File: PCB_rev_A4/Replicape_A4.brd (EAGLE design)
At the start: 100 x 69.6 mm, 189 parts, among them P8 F-2X23-, P9 F-2X23-, Q1 AON6758, Q2 AON6758, Q3 AON6758, Q4 NIF5002, Q5 NIF5002, Q6 NIF5002, U1 SN74AHC595PW, U10 RT8268, U11 PCA9685PW, U12 DAC088S085, U13 DRV8825PWP, U14 DRV8825PWP, U15 DRV8825PWP, U16 DRV8825PWP, U17 DRV8825PWP, U18 CAT24C256, U2 SN74AHC595PW, U3 SN74AHC595PW, U4 SN74AHC595PW, U5 SN74AHC595PW, U6 MCP16321, U7 MCP1402, U8 MCP1402, U9 MCP1402, X1 22-05-7028-02, X10 22-05-7028-02, X11 22-05-7028-02, X12 22-05-7038-03, X13 22-05-7028-02, X14 22-05-7048-04, X15 22-05-7048-04, X16 22-05-7048-04, X17 22-05-7048-04, X18 22-05-7048-04, X19 22-05-7028-02, X2 MSTBA4, X20 MSTBA4, X21 MSTBA2, X23 22-05-7028-02, X3 MSTBA2, X4 22-05-7028-02, X5 22-05-7028-02, X6 22-05-7028-02, X7 22-05-7038-03, X8 22-05-7038-03, X9 22-05-7038-03

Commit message: moved C31
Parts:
- moved R45 1.98 mm to (14.8, 6.14)
- moved LED8 1.83 mm to (14.8, 4.67)
- moved C31 1.30 mm to (22.0, 19.5)
- moved C12 1.02 mm to (18.1, 13.6)
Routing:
- net VDD_IN: track 239.4 -> 242.4 mm
- net DIR_X: track 67.9 -> 68.9 mm
- net GND: vias 194 -> 196
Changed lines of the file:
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@@
 <layer number="42" name="bRestrict" color="1" fill="10" visible="yes" active="yes"/>
 <layer number="43" name="vRestrict" color="2" fill="10" visible="yes" active="yes"/>
-<layer number="44" name="Drills" color="7" fill="1" visible="no" active="yes"/>
+<layer number="44" name="Drills" color="7" fill="1" visible="yes" active="yes"/>
 <layer number="45" name="Holes" color="7" fill="1" visible="yes" active="yes"/>
 <layer number="46" name="Milling" color="3" fill="1" visible="yes" active="yes"/>
@@
 <attribute name="NAME" x="31.0944" y="20.359" size="0.6096" layer="25" rot="R270"/>
 </element>
-<element name="C31" library="rcl" package="C0402" value="0.1uF" x="21.844" y="18.2254" smashed="yes" rot="R270">
-<attribute name="NAME" x="22.4576" y="18.76" size="0.6096" layer="25"/>
+<element name="C31" library="rcl" package="C0402" value="0.1uF" x="21.971" y="19.5208" smashed="yes" rot="R270">
+<attribute name="NAME" x="22.5846" y="20.0554" size="0.6096" layer="25"/>
 </element>
 <element name="C32" library="rcl" package="C0603" value="4.7uF" x="42.625" y="19.4" smashed="yes" rot="R270">
@@
 <attribute name="OC_NEWARK" value="unknown" x="92.625" y="47.875" size="1.778" layer="27" display="off"/>
 </element>
-<element name="C12" library="rcl" package="140CLH-0810" value="100uF" x="18.4" y="14.55" smashed="yes" rot="R90">
-<attribute name="NAME" x="16.745" y="20.235" size="1.27" layer="25" rot="R90"/>
+<element name="C12" library="rcl" package="140CLH-0810" value="100uF" x="18.0698" y="13.5848" smashed="yes" rot="R90">
+<attribute name="NAME" x="16.4148" y="19.2698" size="1.27" layer="25" rot="R90"/>
 </element>
 <element name="C27" library="rcl" package="C0402" value="0.1uF" x="28.7094" y="19.5208" smashed="yes" rot="R270">
@@
 </element>
 <element name="LOGO1" library="ohw-logo" package="OSHW_FILLX200_NOTEXT" value="OSHW_LOGO_FILLX0200-NT" x="43.2584" y="45.9602"/>
-<element name="LED8" library="led" package="CHIP-LED0603" value="red" x="14.875" y="6.5" smashed="yes" rot="R270">
-<attribute name="NAME" x="13.94" y="5.01" size="0.6096" layer="25"/>
+<element name="LED8" library="led" package="CHIP-LED0603" value="red" x="14.7734" y="4.6712" smashed="yes" rot="R270">
+<attribute name="NAME" x="16.2006" y="4.4512" size="0.6096" layer="25"/>
 </element>
-<element name="R45" library="rcl" package="R0402" value="4.7K" x="14.875" y="8.125" smashed="yes">
-<attribute name="NAME" x="16.215" y="8.01" size="0.6096" layer="25"/>
+<element name="R45" library="rcl" package="R0402" value="4.7K" x="14.7734" y="6.1438" smashed="yes">
+<attribute name="NAME" x="16.2658" y="5.851" size="0.6096" layer="25"/>
 </element>
 <element name="F1" library="SparkFun" package="3557" value="3557" x="9.775" y="11.85" rot="R90"/>
@@
 <contactref element="C23" pad="2"/>
 <contactref element="C25" pad="2"/>
-<wire x1="75.725" y1="51.3" x2="75.625" y2="49.125" width="0" layer="19" extent="1-1"/>
+<via x="73.72" y="54.0272" extent="1-16" drill="0.6"/>
+<via x="73.7454" y="52.9096" extent="1-16" drill="0.6"/>
 </signal>
 <signal name="SYS_5V">
@@
 <via x="48.875" y="3.125" extent="1-16" drill="0.3048"/>
 <wire x1="22.125" y1="26.65" x2="22.125" y2="26.625" width="0.1524" layer="1"/>
-<wire x1="22.125" y1="22.375" x2="22.125" y2="26.65" width="0.1524" layer="16"/>
-<wire x1="20.25" y1="20.5" x2="22.125" y2="22.375" width="0.1524" layer="16"/>
-<wire x1="20.25" y1="5" x2="20.25" y2="20.5" width="0.1524" layer="16"/>
-<wire x1="22.125" y1="3.125" x2="20.25" y2="5" width="0.1524" layer="16"/>
+<wire x1="22.125" y1="22.3028" x2="22.125" y2="26.65" width="0.1524" layer="16"/>
+<wire x1="22.125" y1="3.125" x2="20.2438" y2="5.0062" width="0.1524" layer="16"/>
 <via x="22.125" y="26.65" extent="1-16" drill="0.3048"/>
 <contactref element="P8" pad="26"/>
 <wire x1="55.75" y1="9.375" x2="55.835" y2="9.355" width="0.1524" layer="1"/>
+<wire x1="22.125" y1="22.3028" x2="20.9296" y2="21.1074" width="0.1524" layer="16"/>
+<wire x1="20.9296" y1="21.1074" x2="20.1676" y2="21.1074" width="0.1524" layer="16"/>
+<wire x1="20.1676" y1="21.1074" x2="19.6342" y2="20.574" width="0.1524" layer="16"/>
+<wire x1="19.6342" y1="20.574" x2="19.6342" y2="19.4056" width="0.1524" layer="16"/>
+<wire x1="19.6342" y1="19.4056" x2="20.2438" y2="18.796" width="0.1524" layer="16"/>
+<wire x1="20.2438" y1="18.796" x2="20.2438" y2="5.0062" width="0.1524" layer="16"/>
 </signal>
 <signal name="STEP_X">
@@
 <wire x1="13.125" y1="18" x2="14.125" y2="18" width="2" layer="1"/>
 <wire x1="14.125" y1="18" x2="17.125" y2="18" width="2" layer="1"/>
-<wire x1="17.125" y1="18" x2="18.4" y2="17.8" width="0.4" layer="1"/>
 <polygon width="0.1542" layer="1" isolate="0.5">
 <vertex x="13.375" y="11.5"/>
@@
 <vertex x="13.375" y="21.75"/>
 </polygon>
-<wire x1="14.225" y1="8.125" x2="14.125" y2="8.125" width="0.4" layer="1"/>
+<wire x1="14.1234" y1="6.1438" x2="14.125" y2="8.125" width="0.4" layer="1"/>
 <wire x1="14.125" y1="18" x2="14.125" y2="8.125" width="0.4" layer="1"/>
-<wire x1="17.125" y1="17.75" x2="18.4" y2="17.8" width="0.4" layer="1"/>
+<wire x1="17.125" y1="17.75" x2="18.0698" y2="16.8348" width="0.4" layer="1"/>
 <wire x1="52.525" y1="20.1" x2="51.75" y2="20.125" width="1.4224" layer="16"/>
 <wire x1="51.75" y1="20.125" x2="51.625" y2="20.125" width="0.8192" layer="16"/>
@@
 <wire x1="39.625" y1="20.125" x2="34.5" y2="20.125" width="1.4224" layer="16"/>
 <wire x1="34.5" y1="20.125" x2="27.625" y2="20.125" width="1.4224" layer="16"/>
-<wire x1="27.625" y1="20.125" x2="21.875" y2="20.125" width="1.4224" layer="16"/>
-<via x="21.875" y="20.125" extent="1-16" drill="0.6"/>
+<wire x1="27.625" y1="20.125" x2="20.6812" y2="20.125" width="1.4224" layer="16"/>
+<via x="20.6812" y="20.125" extent="1-16" drill="0.6"/>
 <wire x1="39.375" y1="20.375" x2="39.375" y2="21.75" width="0.4096" layer="1"/>
 <wire x1="39.625" y1="20.125" x2="39.375" y2="20.375" width="0.4096" layer="1"/>
@@
 <wire x1="80.25" y1="46.75" x2="80.225" y2="46.7" width="0.1524" layer="1"/>
 <wire x1="80.25" y1="47.125" x2="80.225" y2="47.2" width="0.1524" layer="1"/>
-<wire x1="18.75" y1="18.125" x2="18.4" y2="17.8" width="0.1524" layer="1"/>
 <wire x1="83.25" y1="47.25" x2="83.75" y2="47.25" width="0.254" layer="1"/>
 <wire x1="83.75" y1="47.25" x2="83.875" y2="47.125" width="0.254" layer="1"/>
@@
 <via x="60.875" y="49.375" extent="1-16" drill="0.305"/>
 <via x="77.75" y="40.625" extent="1-16" drill="0.7"/>
-<wire x1="22.875" y1="21.125" x2="22.875" y2="21.75" width="0.4064" layer="1"/>
-<wire x1="21.875" y1="20.125" x2="22.875" y2="21.125" width="0.4064" layer="1"/>
+<wire x1="22.875" y1="20.521" x2="22.875" y2="21.75" width="0.4064" layer="1"/>
 <wire x1="22.875" y1="21.75" x2="22.85" y2="21.7875" width="0.4064" layer="1"/>
 <polygon width="0.1542" layer="16" isolate="0.5">
@@
 <wire x1="27.625" y1="20.125" x2="28.7094" y2="20.125" width="0.4096" layer="1"/>
 <wire x1="28.7094" y1="20.125" x2="28.7094" y2="20.1708" width="0.4096" layer="1"/>
-<wire x1="21.875" y1="20.125" x2="21.844" y2="20.125" width="0.4096" layer="1"/>
-<wire x1="21.844" y1="20.125" x2="21.844" y2="18.8754" width="0.4096" layer="1"/>
 <wire x1="22.85" y1="21.7875" x2="22.85" y2="22.55" width="0.1524" layer="1"/>
 <wire x1="22.85" y1="22.55" x2="20" y2="25.4" width="0.1524" layer="1"/>
@@
 <wire x1="56.2" y1="26.6" x2="55.375" y2="26.6" width="0.1524" layer="1"/>
 <wire x1="55.375" y1="26.6" x2="55.3504" y2="26.9278" width="0.1524" layer="1"/>
-<wire x1="18.75" y1="18.125" x2="18.75" y2="18.55" width="1.4224" layer="1"/>
-<wire x1="18.75" y1="18.55" x2="20.3" y2="20.1" width="1.4224" layer="1"/>
-<wire x1="20.3" y1="20.1" x2="21.85" y2="20.1" width="1.4224" layer="1"/>
-<wire x1="21.85" y1="20.1" x2="21.875" y2="20.125" width="1.4224" layer="1"/>
 <wire x1="79.375" y1="39" x2="81" y2="39" width="0.8128" layer="1"/>
 <wire x1="81" y1="39" x2="81" y2="29.4" width="0.8128" layer="1"/>
@@
 <wire x1="79.289" y1="23.717" x2="79.195" y2="23.717" width="0.8128" layer="1"/>
 <wire x1="79.195" y1="23.717" x2="79.1" y2="23.622" width="0.8128" layer="1"/>
+<wire x1="17.125" y1="18" x2="18.0698" y2="18" width="1.9812" layer="1"/>
+<wire x1="18.0698" y1="18" x2="18.0698" y2="16.8348" width="1.9812" layer="1"/>
+<wire x1="20.6248" y1="20.125" x2="20.1948" y2="20.125" width="1.4224" layer="1"/>
+<wire x1="20.1948" y1="20.125" x2="18.0698" y2="18" width="1.4224" layer="1"/>
+<wire x1="22.875" y1="20.521" x2="22.479" y2="20.125" width="0.4064" layer="1"/>
+<wire x1="22.479" y1="20.125" x2="22.0168" y2="20.125" width="0.4064" layer="1"/>
+<wire x1="22.0168" y1="20.125" x2="21.971" y2="20.1708" width="0.4064" layer="1"/>
+<wire x1="20.6812" y1="20.125" x2="21.9252" y2="20.125" width="0.4064" layer="1"/>
+<wire x1="21.9252" y1="20.125" x2="21.971" y2="20.1708" width="0.4064" layer="1"/>
+<wire x1="20.6248" y1="20.125" x2="20.6812" y2="20.125" width="0.4064" layer="1"/>
 </signal>
 <signal name="VDD_5V">
@@
 <vertex x="0" y="0"/>
 </polygon>
-<wire x1="13.375" y1="6.5" x2="14.125" y2="6.5" width="0.254" layer="1"/>
+<wire x1="13.2226" y1="4.6712" x2="14.0234" y2="4.6712" width="0.254" layer="1"/>
 </signal>
 <signal name="N$23">
@@
 <contactref element="LED8" pad="C"/>
 <contactref element="R45" pad="2"/>
-<wire x1="15.5" y1="6.625" x2="15.625" y2="6.5" width="0.254" layer="1"/>
-<wire x1="15.5" y1="6.625" x2="15.525" y2="8.125" width="0.254" layer="1"/>
+<wire x1="15.5" y1="6.1424" x2="15.5234" y2="4.6712" width="0.254" layer="1"/>
+<wire x1="15.5" y1="6.1424" x2="15.4234" y2="6.1438" width="0.254" layer="1"/>
 </signal>
 <signal name="N$10">

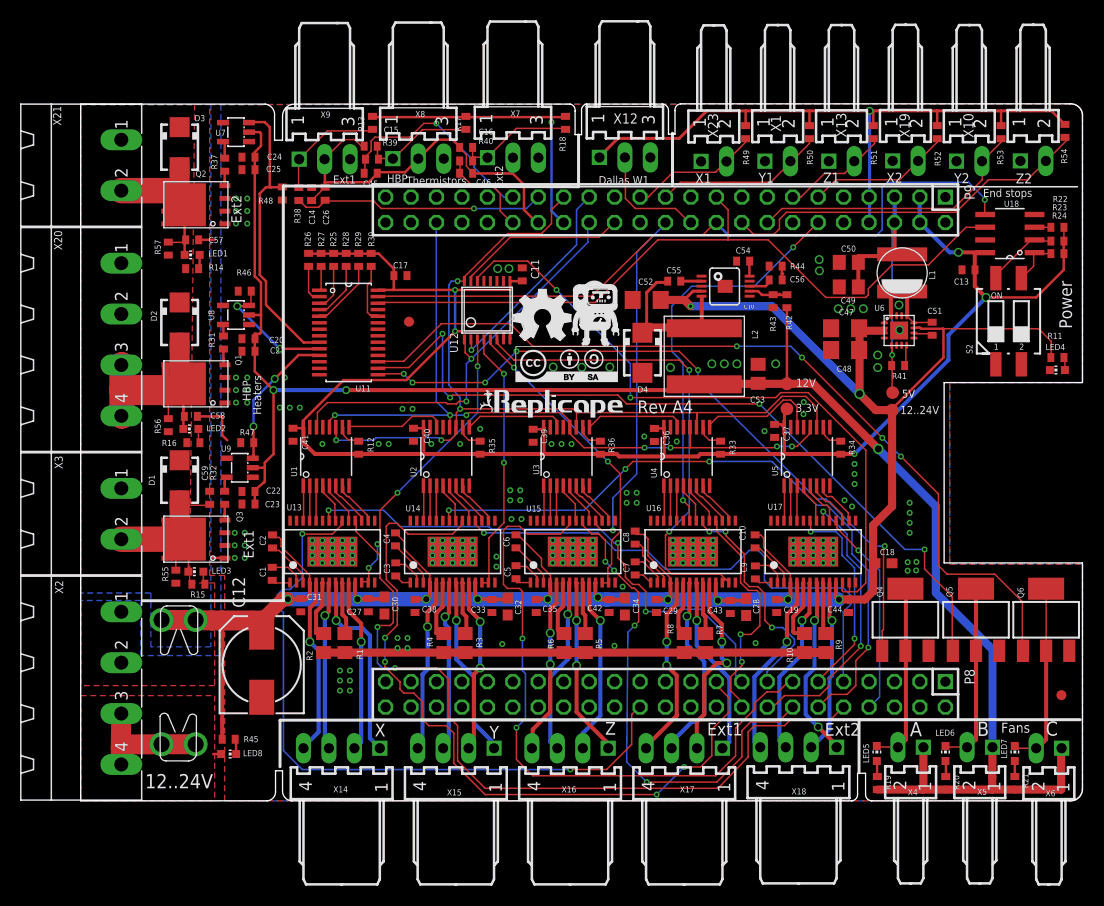
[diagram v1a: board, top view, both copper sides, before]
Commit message: Changed the pullup VDD from 5V to 3.3V
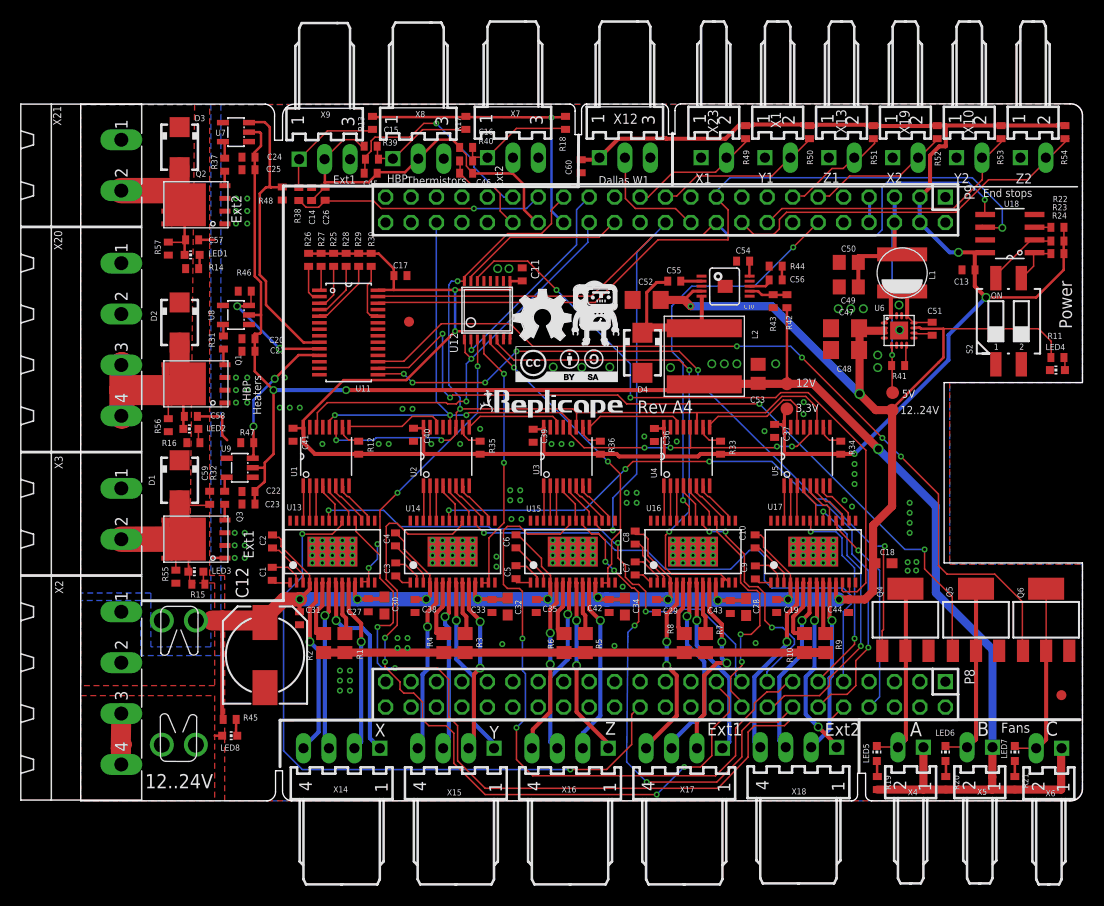
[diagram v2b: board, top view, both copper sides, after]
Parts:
- added C60: 0.47uF, rcl:C0402
- F1: value 3557 -> FUSE3557; device SparkFun:3557 -> fuse:3557
- moved R45 1.98 mm to (14.9, 8.12)
- moved LED8 1.83 mm to (14.9, 6.50)
- moved C31 1.30 mm to (21.8, 18.2)
- moved C12 1.02 mm to (18.4, 14.6)
- moved X23 0.38 mm to (63.2, 64.2)
- moved X1 0.35 mm to (69.6, 64.2)
- moved X10 0.35 mm to (88.7, 64.2)
- moved X13 0.35 mm to (76.0, 64.2)
- moved X11 0.33 mm to (95.1, 64.2)
- moved X19 0.33 mm to (82.3, 64.2)
- moved R54 0.12 mm to (98.2, 66.8)
- moved F1 0.06 mm to (9.80, 11.8)
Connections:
- net +3V3: now also C60.1, R49.2, R50.2, R51.2, R52.2, R53.2, R54.2, X12.1
- net GND: now also C60.2
- net SYS_5V: no longer R49.2, R50.2, R51.2, R52.2, R53.2, R54.2, X12.1
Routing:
- net SYS_5V: track 68.2 -> 3.10 mm, vias 1 -> 0
- net +3V3: track 183.6 -> 242.7 mm
- net VDD_IN: track 242.4 -> 234.3 mm
- net VIN: track 13.5 -> 6.46 mm
- net I2C2_SCL: track 73.7 -> 77.6 mm, vias 0 -> 1
- net N$234: track 31.6 -> 30.2 mm
- net N$242: track 31.8 -> 30.7 mm
- net DIR_X: track 68.9 -> 67.9 mm
- net END_STOP_Y_2: track 28.6 -> 29.2 mm
- net END_STOP_X_1: track 13.3 -> 14.0 mm
- net GND: vias 196 -> 194

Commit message: working on fixing the pipes
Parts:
- moved C50 4.21 mm to (75.6, 49.7), turned to 270 degrees
- moved C47 2.63 mm to (75.6, 44.6), turned to 90 degrees
- moved C49 1.95 mm to (77.8, 49.7), turned to 270 degrees
- moved C48 1.54 mm to (77.8, 44.6), turned to 90 degrees
- moved L1 0.71 mm to (81.5, 52.2), turned to 270 degrees
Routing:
- net SW: track 10.3 -> 12.7 mm
- net VDD_IN: track 234.3 -> 235.8 mm
- net VDD_5V: track 32.7 -> 33.2 mm, vias 1 -> 2

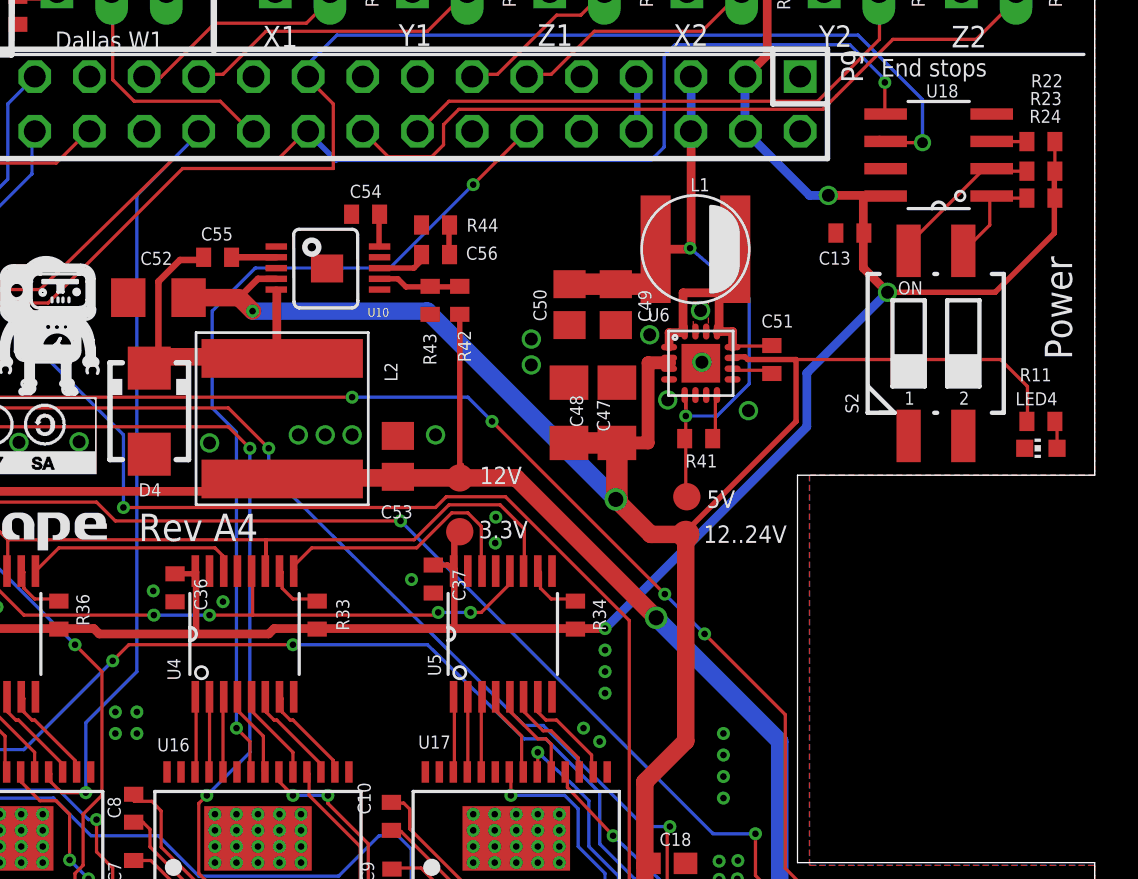
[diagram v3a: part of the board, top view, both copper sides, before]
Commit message: Added a cap across 5V for stability.
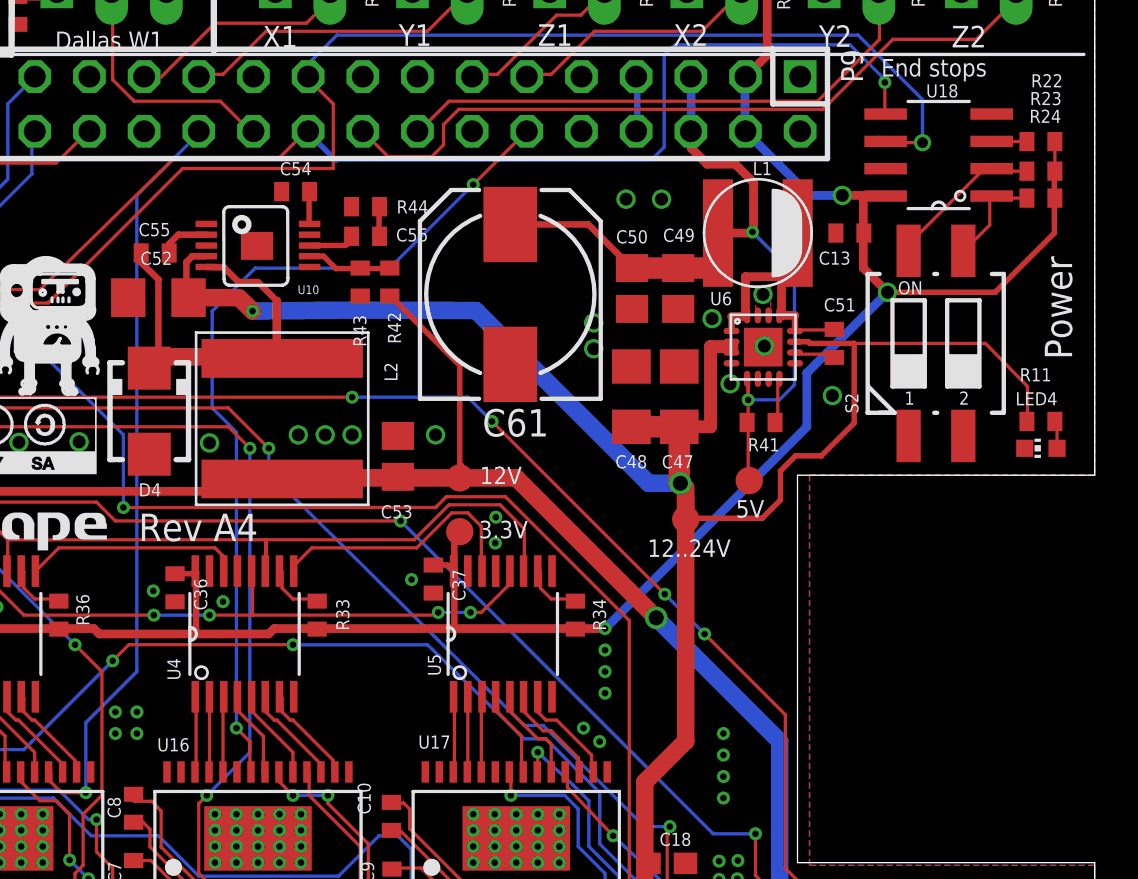
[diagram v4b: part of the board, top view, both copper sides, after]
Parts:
- added C61: 100uF, rcl:140CLH-0810
- moved C54 3.42 mm to (62.9, 54.9)
- moved U10 3.42 mm to (61.1, 52.4)
- moved C56 3.36 mm to (66.1, 52.9)
- moved R42 3.36 mm to (67.2, 50.7)
- moved R43 3.36 mm to (65.9, 50.7)
- moved R44 3.36 mm to (66.1, 54.2)
- moved 5V 3.00 mm to (84.0, 41.5)
- moved C48 3.00 mm to (80.7, 45.4)
- moved C49 3.00 mm to (80.7, 50.4)
- moved C50 3.00 mm to (78.5, 50.4)
- moved C51 3.00 mm to (87.9, 47.9)
- moved R41 3.00 mm to (84.5, 44.2)
- moved C47 3.00 mm to (78.5, 45.4)
- moved L1 3.00 mm to (84.3, 53.0)
- moved U6 3.00 mm to (84.6, 47.7)
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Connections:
- net GND: now also C61.-
- net VDD_5V: now also C61.+
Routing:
- net VDD_5V: track 33.2 -> 40.1 mm
- net VDD_IN: track 235.8 -> 240.5 mm
- net N$238: track 17.3 -> 19.7 mm
- net VDD_12V: track 181.5 -> 183.7 mm
- net GND: vias 194 -> 196
